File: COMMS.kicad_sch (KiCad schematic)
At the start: 2 parts

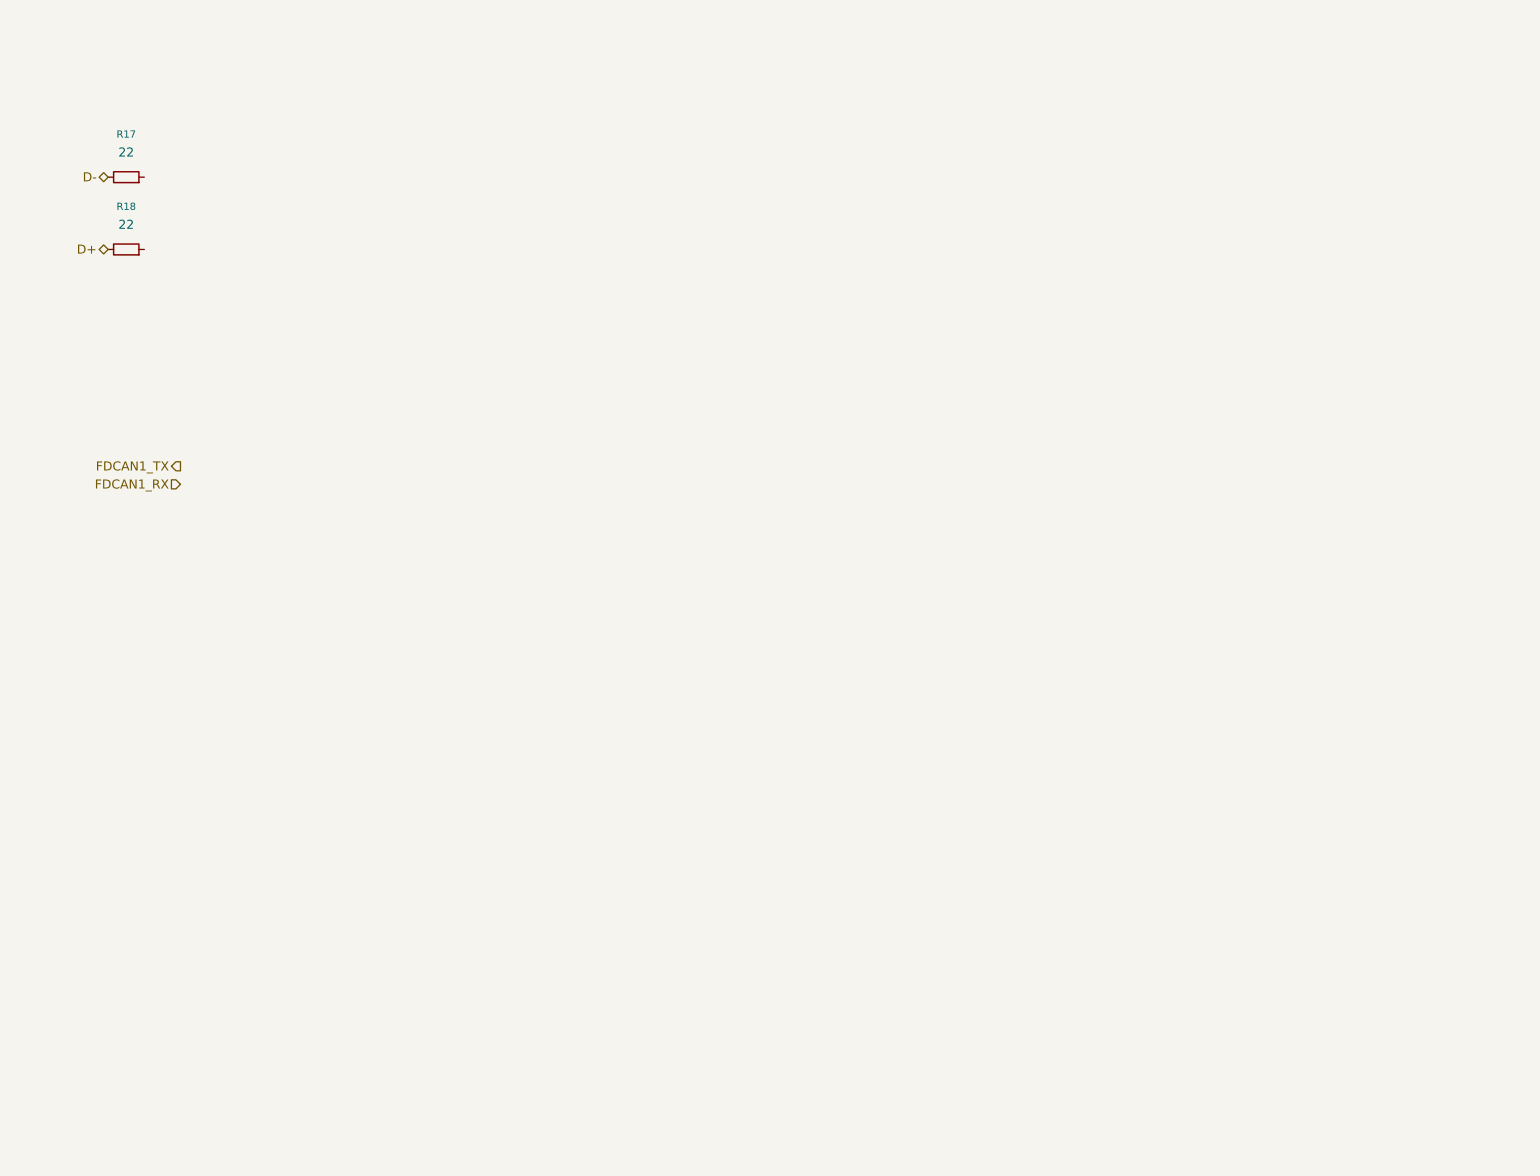
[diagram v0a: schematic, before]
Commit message: added in RF componentys and updated and reviewed STM connections
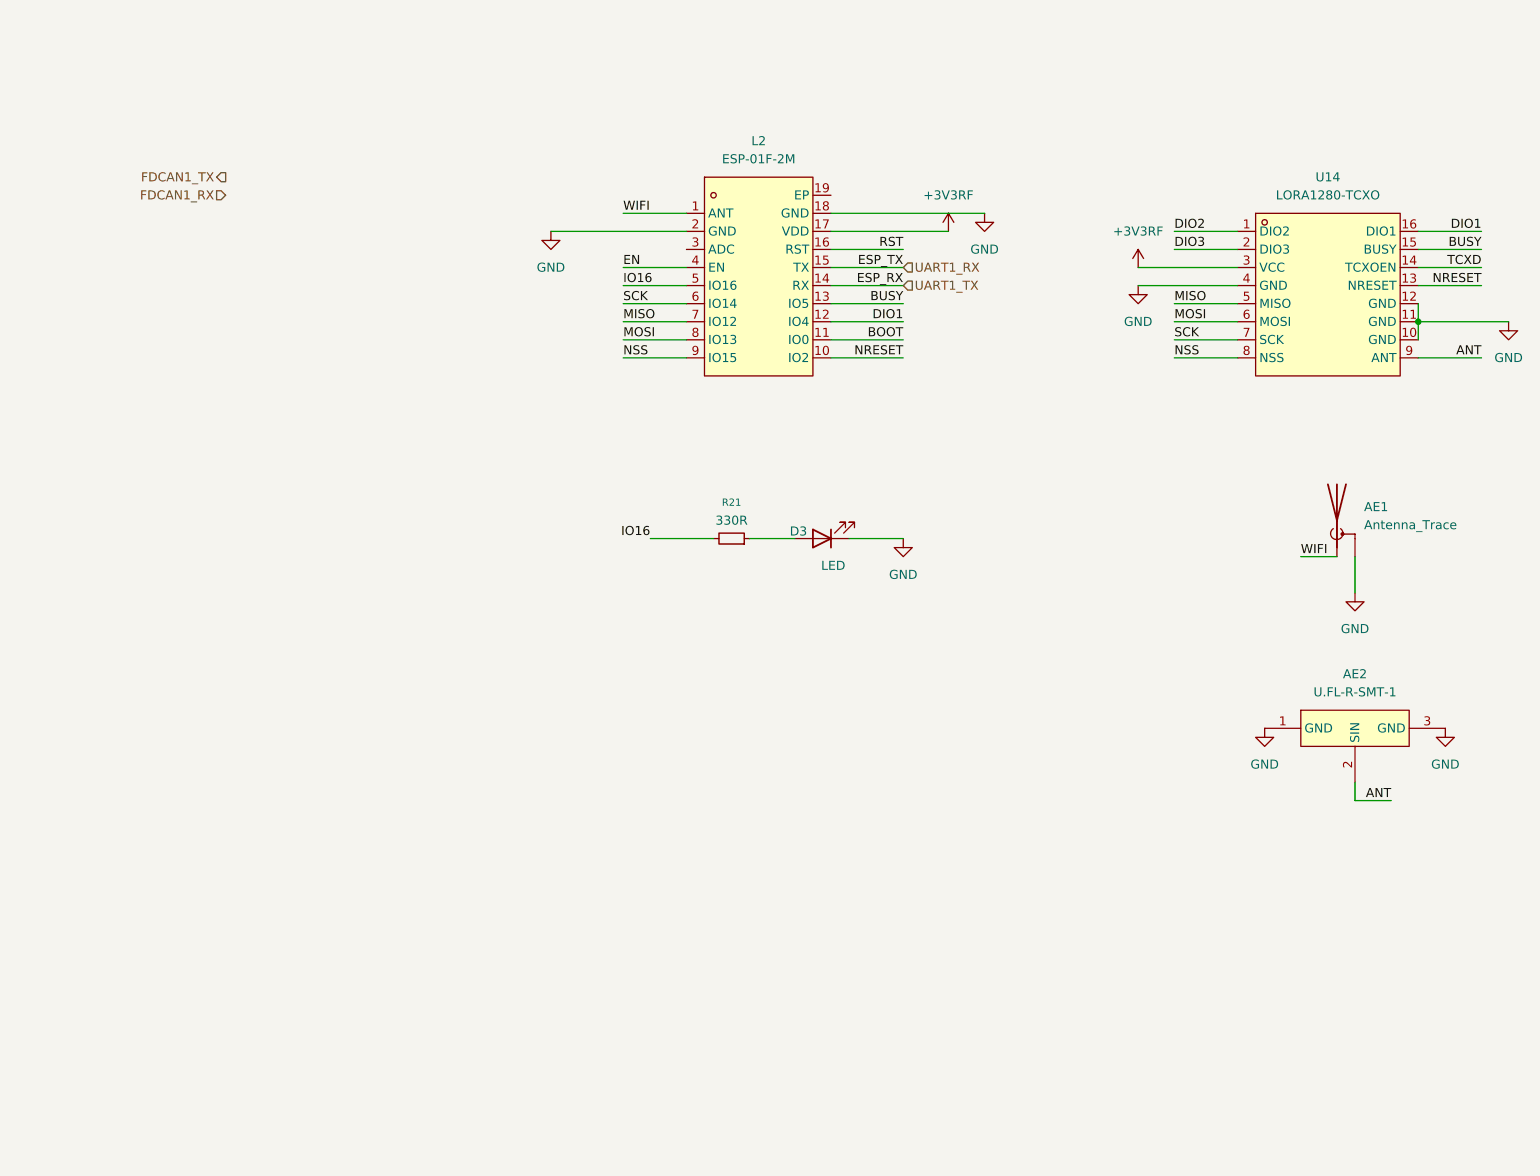
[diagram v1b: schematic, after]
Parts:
- removed R17, R18: 22, Resistor_SMD:R_0201_0603Metric, symbol Device:R_Small
- added AE1: Antenna_Trace, symbol Device:Antenna_Shield
- added AE2: U.FL-R-SMT-1, LCSC:ANT-SMD_UFL-R-SMT-1-10, symbol LCSC:U.FL-R-SMT-1
- added D3: LED, symbol Device:LED
- added L2: ESP-01F-2M, LCSC:WIFIM-SMD_ESP-01F-2M, symbol LCSC:ESP-01F-2M
- added R21: 330R, Resistor_SMD:R_0201_0603Metric, symbol Device:R_Small
- added U14: LORA1280-TCXO, LCSC:WIRELM-SMD_16P-L16.0-W16.0-P2.00_LORA1280-TCXO, symbol LCSC:LORA1280-TCXO
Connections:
- new net: D3.2 (A), R21.1
- new net +3V3RF: L2.17 (VDD), U14.3 (VCC)
- new net ANT: AE2.2 (SIN), U14.9 (ANT)
- new net BOOT: L2.11 (IO0)
- new net BUSY: L2.13 (IO5), U14.15 (BUSY)
- new net DIO1: L2.12 (IO4), U14.16 (DIO1)
- new net DIO2: U14.1 (DIO2)
- new net DIO3: U14.2 (DIO3)
- new net EN: L2.4 (EN)
- new net GND: AE1.2 (Shield), AE2.1 (GND), AE2.3 (GND), D3.1 (K), L2.18 (GND), L2.2 (GND), U14.10 (GND), U14.11 (GND), U14.12 (GND), U14.4 (GND)
- new net IO16: L2.5 (IO16), R21.2
- new net MISO: L2.7 (IO12), U14.5 (MISO)
- new net MOSI: L2.8 (IO13), U14.6 (MOSI)
- new net NRESET: L2.10 (IO2), U14.13 (NRESET)
- new net NSS: L2.9 (IO15), U14.8 (NSS)
- new net RST: L2.16 (RST)
- new net SCK: L2.6 (IO14), U14.7 (SCK)
- new net TCXD: U14.14 (TCXOEN)
- new net UART1_RX: L2.15 (TX)
- new net UART1_TX: L2.14 (RX)
- new net WIFI: AE1.1 (A), L2.1 (ANT)

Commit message: finalized RF
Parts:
- added C51, C57, C60: 100nF, Capacitor_SMD:C_0201_0603Metric_Pad0.64x0.40mm_HandSolder, symbol Device:C_Small
- added C55: 22uF, Capacitor_SMD:C_0201_0603Metric_Pad0.64x0.40mm_HandSolder, symbol Device:C_Small
- added C56: 10uF, Capacitor_SMD:C_0201_0603Metric_Pad0.64x0.40mm_HandSolder, symbol Device:C_Small
- added C59: 1uF, Capacitor_SMD:C_0201_0603Metric_Pad0.64x0.40mm_HandSolder, symbol Device:C_Small
- added CN4: FTSH-107-01-L-DV-K, LCSC:HDR-SMD_14P-P1.27_FTSH-107-01-L-DV-K, symbol LCSC:FTSH-107-01-L-DV-K
- added JP2: Jumper_3_Open, symbol Jumper:Jumper_3_Open
- added JP3, JP4: Jumper_2_Open, symbol Jumper:Jumper_2_Open
- added R22, R23: 10k, Resistor_SMD:R_0201_0603Metric, symbol Device:R_Small
- added R24: 470R, Resistor_SMD:R_0201_0603Metric, symbol Device:R_Small
- added R25, R26: 330R, Resistor_SMD:R_0201_0603Metric, symbol Device:R_Small
- added SW1: SW_Push, symbol Switch:SW_Push
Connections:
- net +3V3RF: now also C55.1, C56.1, C57.1, C59.1, C60.1, CN4.01 (1), JP2.3 (B), R22.1, R23.1, R24.1
- net BOOT: now also SW1.1
- net EN: now also R22.2
- net GND: now also L2.19 (EP), C51.2, C55.2, C56.2, C57.2, C59.2, C60.2, CN4.04 (4), JP2.1 (A), SW1.2
- net RST: now also C51.1, R23.2
- net UART1_RX: now also JP3.2 (B); no longer L2.15 (TX)
- net UART1_TX: now also JP4.2 (B); no longer L2.14 (RX)
- net TCXD renamed TCXO
- net TCXO: now also JP2.2 (C)
- new net: JP3.1 (A), R25.1
- new net: JP4.1 (A), R26.1
- new net ESP_RX: CN4.03 (3), L2.14 (RX), R26.2
- new net ESP_TX: CN4.02 (2), L2.15 (TX), R24.2, R25.2
